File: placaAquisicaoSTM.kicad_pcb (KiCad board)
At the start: 2 copper layers, 102 x 80 mm, 82 parts, among them IC1 STM32H523CET6, J1 Conn_01x05, J2 Conn_02x06_Top_Bottom, SW1 SW_SPDT, SW2 SW_Push, U1 PC817, U2 PC817, U3 PC817, U4 LMV321, U5 LMV321, U6 74HC14, U7 AMS1117-5.0, U8 AMS1117-3.3, U9 SN65HVD230, Y1 Crystal, Y2 Crystal_GND23

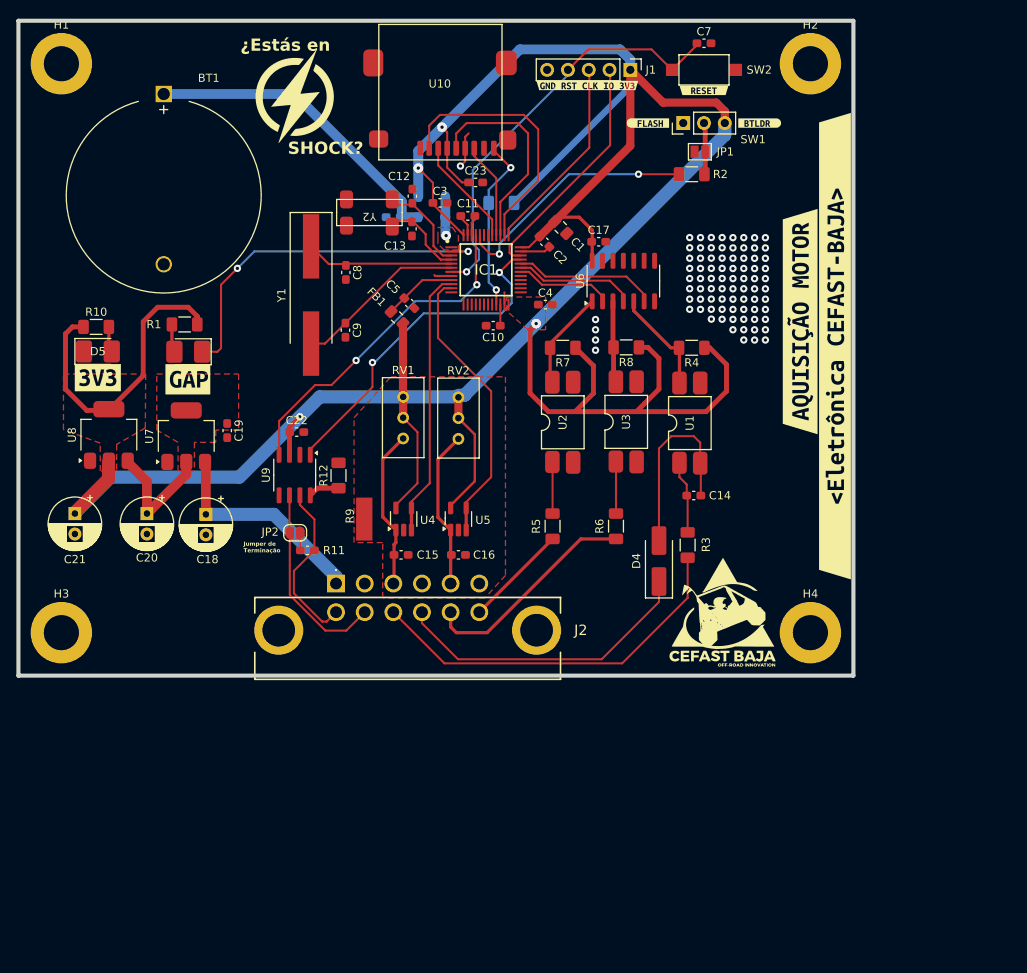
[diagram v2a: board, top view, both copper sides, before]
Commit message: Diminui o tamanho da placa
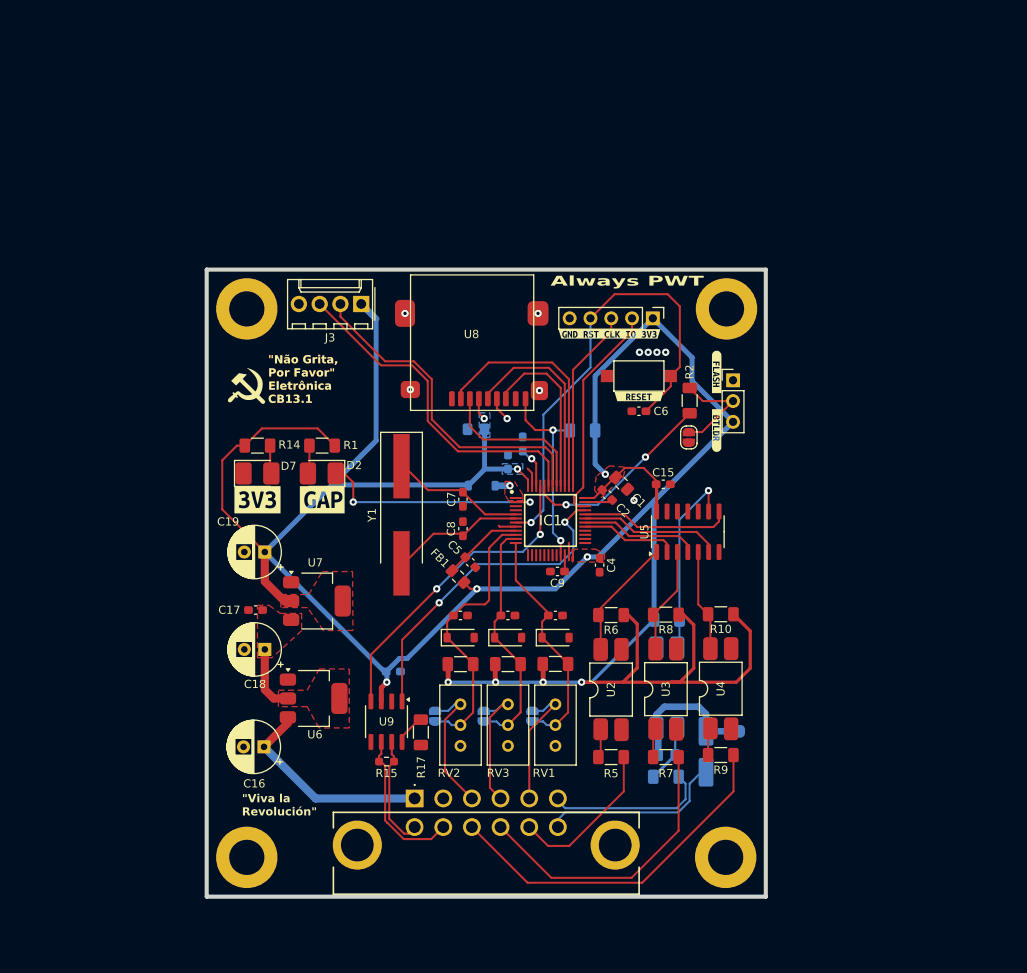
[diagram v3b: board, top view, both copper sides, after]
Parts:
- removed BT1: Battery_Cell, Battery:BatteryHolder_MYOUNG_BS-07-A1BJ001_CR2032
- removed the C12 at (111.6, 66.4)
- removed the C16 at (117.2, 110.2)
- removed C23: 1n, Capacitor_SMD:C_0603_1608Metric_Pad1.08x0.95mm_HandSolder
- removed the C6 at (109.3, 69.0)
- removed the D2 at (114.0, 69.0)
- removed the G*** at (97.2, 54.2)
- removed the G*** at (149.5, 117.2)
- removed the G*** at (142.8, 106.0)
- removed U10: ~, Baja_Library:SD-CARD-GENERIC
- removed the U5 at (117.2, 105.9)
- removed Y2: Crystal_GND23, Baja_Library:DMX-26S
- removed kibuzzard-6758F1AD: G***, kibuzzard-6758F1AD
- removed kibuzzard-6758F709: G***, kibuzzard-6758F709
- removed kibuzzard-6758F727: G***, kibuzzard-6758F727
- removed kibuzzard-67891694: G***, kibuzzard-67891694
- removed kibuzzard-67897D6F: G***, kibuzzard-67897D6F
- added C14: 1n, Capacitor_SMD:C_0603_1608Metric_Pad1.08x0.95mm_HandSolder, F.Cu at (129.1, 117.7)
- added C20: 1n, Capacitor_SMD:C_0805_2012Metric_Pad1.18x1.45mm_HandSolder, B.Cu at (119.4, 94.9)
- added D4: D_Zener, Diode_SMD:D_SOD-123, F.Cu at (117.5, 120.4)
- added D5: D_Zener, Diode_SMD:D_SOD-123, F.Cu at (123.3, 120.4)
- added D6: D_Zener, Diode_SMD:D_SOD-123, F.Cu at (129.1, 120.4)
- added G***: LOGO, Baja_Library:communism, F.Cu at (91.3, 89.6)
- added J3: Conn_01x04, Baja_Library:Molex_KK-254_AE-6410-04A_1x04_P2.54mm_Vertical, F.Cu at (105.4, 79.6)
- added JP6: SolderJumper_2_Open, Jumper:SolderJumper-2_P1.3mm_Open_RoundedPad1.0x1.5mm, B.Cu at (114.4, 129.9)
- added JP7: SolderJumper_2_Open, Jumper:SolderJumper-2_P1.3mm_Open_RoundedPad1.0x1.5mm, B.Cu at (120.3, 129.9)
- added JP8: SolderJumper_2_Open, Jumper:SolderJumper-2_P1.3mm_Open_RoundedPad1.0x1.5mm, B.Cu at (126.3, 129.9)
- added R10: 10k, Resistor_SMD:R_1206_3216Metric_Pad1.30x1.75mm_HandSolder, F.Cu at (149.3, 117.5)
- added R12: 27k, Resistor_SMD:R_1206_3216Metric_Pad1.30x1.75mm_HandSolder, F.Cu at (123.3, 123.6)
- added R15: 120, Resistor_SMD:R_0603_1608Metric_Pad0.98x0.95mm_HandSolder, F.Cu at (108.5, 135.5)
- added R16: 10K, Resistor_SMD:R_1206_3216Metric_Pad1.30x1.75mm_HandSolder, B.Cu at (132.4, 95.0)
- added RV3: 10k_trim, Potentiometer_THT:Potentiometer_Bourns_3296W_Vertical, F.Cu at (123.3, 128.5)
- added U8: ~, Baja_Library:SD-CARD-GENERIC, F.Cu at (118.8, 86.1)
- added kibuzzard-67EDAA6F: G***, kibuzzard-67EDAA6F, F.Cu at (100.6, 103.5)
- C10: renamed from C11; moved to B.Cu
- C11: renamed from C14; footprint Capacitor_SMD:C_0603_1608Metric_Pad1.08x0.95mm_HandSolder -> Capacitor_SMD:C_0805_2012Metric_Pad1.18x1.45mm_HandSolder; moved to B.Cu
- C13: value 22p -> 1n
- C21: renamed from C22; moved to B.Cu
- C3, H3, JP2, R3, R4, U1: moved to B.Cu
- D3: renamed from D4; moved to B.Cu
- JP1: footprint Jumper:SolderJumper-2_P1.3mm_Open_Pad1.0x1.5mm -> Jumper:SolderJumper-2_P1.3mm_Open_RoundedPad1.0x1.5mm
- R11: value 120 -> 27k; footprint Capacitor_SMD:C_0603_1608Metric_Pad1.08x0.95mm_HandSolder -> Resistor_SMD:R_1206_3216Metric_Pad1.30x1.75mm_HandSolder
- R13: value 10k -> 27k; moved to F.Cu
- R9: value 0R -> 680; footprint Baja_Library:JumperPotencia -> Resistor_SMD:R_1206_3216Metric_Pad1.30x1.75mm_HandSolder
- U4: value LMV321 -> PC817; footprint Package_TO_SOT_SMD:SOT-23-5_HandSoldering -> Baja_Library:SO-4_HandSoldering
- moved JP2 59.0 mm to (151.1, 131.8)
- moved R13 56.7 mm to (129.1, 123.6)
- moved R9 52.3 mm to (149.3, 134.7), turned to 180 degrees
- moved C13 48.7 mm to (123.3, 117.7), turned to 0 degrees
- moved G*** 47.4 mm to (96.7, 88.4)
- moved C6 45.6 mm to (139.3, 92.7), turned to 180 degrees
- moved U4 43.9 mm to (149.3, 126.6)
- moved RV1 41.9 mm to (129.1, 128.5)
- moved SW2 38.2 mm to (139.3, 88.4), turned to 0 degrees
- moved kibuzzard-67572B0D 38.2 mm to (139.3, 90.9)
- moved kibuzzard-67572AD3 37.9 mm to (148.8, 95.1), turned to -90 degrees
- moved H1 37.6 mm to (91.4, 80.2)
- moved RV2 37.5 mm to (117.5, 128.5)
- moved D1 35.8 mm to (120.1, 101.8)
- moved U6 35.6 mm to (99.6, 127.8), turned to 0 degrees
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- renumbered C15 to C12, C17 to C15, C18 to C16, C19 to C17, C20 to C18, C21 to C19, C7 to C6, C8 to C7, C9 to C8, C10 to C9, D3 to D2, D5 to D7, R10 to R14, R12 to R17, R7 to R6, R6 to R7, U6 to U5, U7 to U6, U8 to U7
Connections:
- C11 pad 2: Net-(D4-A) -> JMP_RPM
- C12 pad 1: NTC_P1 -> NTC_AN_1
- C12 pad 2: NTC_N1 -> GND
- C13 pad 1: /MicroControlador/LSE_OUT -> NTC_AN_2
- D3 pad 1: MTMT -> MT+
- D3 pad 2: Net-(D4-A) -> JMP_RPM
- IC1 pad 12: unconnected-(IC1-PA2-Pad12) -> NTC_AN_3
- IC1 pad 21: SD_ON -> SD_DET
- IC1 pad 29: unconnected-(IC1-PA8-Pad29) -> DIG3
- IC1 pad 3: /MicroControlador/LSE_IN -> unconnected-(IC1-PC14-OSC32_IN-Pad3)
- IC1 pad 38: CS_SD -> SD_CS
- IC1 pad 4: /MicroControlador/LSE_OUT -> unconnected-(IC1-PC15-OSC32_OUT-Pad4)
- J2 pad 10: MTMT -> OPTO_IN_1
- J2 pad 11: OPTO_IN_1 -> OPTO_IN_0
- J2 pad 12: OPTO_IN_0 -> MT+
- J2 pad 4: NTC_N1 -> NTC_P2
- J2 pad 5: NTC_P2 -> NTC_P3
- J2 pad 6: NTC_N1 -> MT-
- J2 pad 9: CHASSI -> OPTO_IN_2
- JP2 pad 1: CAN- -> JMP_RPM
- JP2 pad 2: Net-(JP2-B) -> GND
- R11 pad 1: CAN+ -> +3V3
- R11 pad 2: Net-(JP2-B) -> NTC_AN_1
- R13 pad 1: SD_ON -> +3V3
- R13 pad 2: +3V3 -> NTC_AN_3
- R3 pad 1: CHASSI -> MT-
- R9 pad 1: GND -> OPTO_IN_2
- R9 pad 2: NTC_N1 -> Net-(R9-Pad2)
- RV1 pad 1: +3V3 -> NTC_P3
- RV1 pad 2: +3V3 -> NTC_AN_3
- RV1 pad 3: NTC_P1 -> GND
- RV2 pad 1: +3V3 -> NTC_P1
- RV2 pad 2: +3V3 -> NTC_AN_1
- RV2 pad 3: NTC_P2 -> GND
- U1 pad 2: Net-(D4-A) -> JMP_RPM
- U4 pad 1: NTC_P1 -> Net-(R9-Pad2)
- U4 pad 2: NTC_N1 -> GND
- U4 pad 3: NTC_AN_1 -> GND
- U4 pad 4: NTC_AN_1 -> OPTO_2
- U5 pad 2: DIG2 -> DIG3
- U5 pad 4: DIG1 -> DIG2
- U5 pad 5: RPM -> OPTO_2
- U5 pad 6: DIG0 -> DIG1
- U5 pad 8: (no net) -> DIG0
- U5 pad 9: (no net) -> RPM
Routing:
- net CHASSI: track 46.8 -> 0.00 mm
- net OPTO_IN_2: track 0.00 -> 43.8 mm
- net RX1: track 0.00 -> 41.8 mm
- net TX1: track 0.00 -> 41.1 mm
- net Net-(BT1-+): track 38.5 -> 0.00 mm
- net MTMT: track 37.5 -> 0.00 mm
- net CS_SD: track 32.0 -> 0.00 mm
- net SD_CS: track 0.00 -> 29.5 mm
- net NTC_AN_3: track 0.00 -> 29.1 mm
- net SD_DET: track 0.00 -> 24.2 mm, vias 0 -> 2
- net Net-(D4-A): track 23.7 -> 0.00 mm
- net MT+: track 0.00 -> 22.6 mm
- net SD_ON: track 21.4 -> 0.00 mm, vias 2 -> 0
- net MT-: track 0.00 -> 19.8 mm
- net JMP_RPM: track 0.00 -> 16.9 mm
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- added copper zone on B.Cu, net +3V3
- removed copper zone on F.Cu, net NTC_N1
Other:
- board size 102 x 80 mm -> 68.3 x 76.6 mm
- board text added: "Always PWT"
- board text added: "{dblquote}Não Grita, Por Favor{dblquote} Eletrônica CB13.1"
- board text added: "{dblquote}Se eu ouvisse o que eles dizem não fazia nada, O que eles dizem não derruba minha parada{dblquote}"
- board text added: "{dblquote}Viva la Revolución{dblquote}"
- board text removed: "I LOVE PWT"
- board text removed: "Jumper de Terminação"
- board text removed: "SHOCK?"
- board text removed: "¿Estás en"

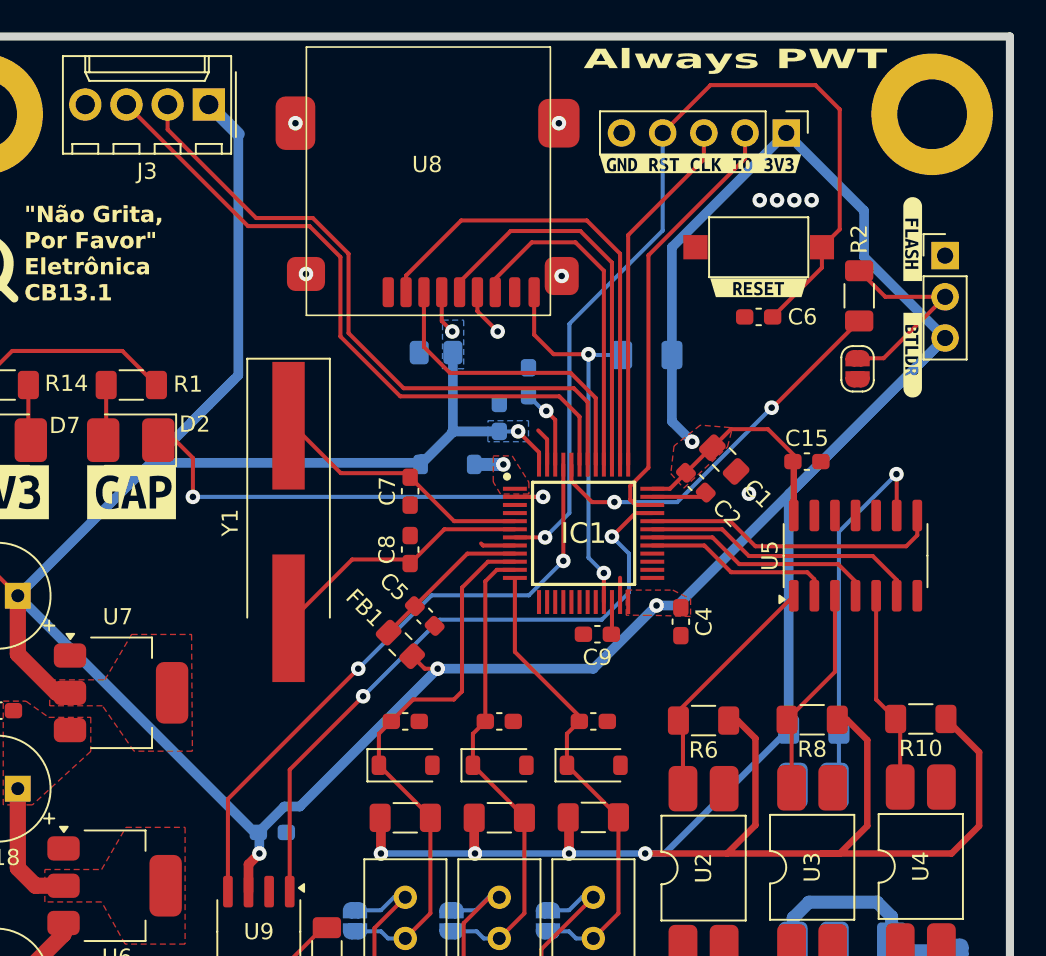
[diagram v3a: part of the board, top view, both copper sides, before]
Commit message: Removi o botao de reset do design
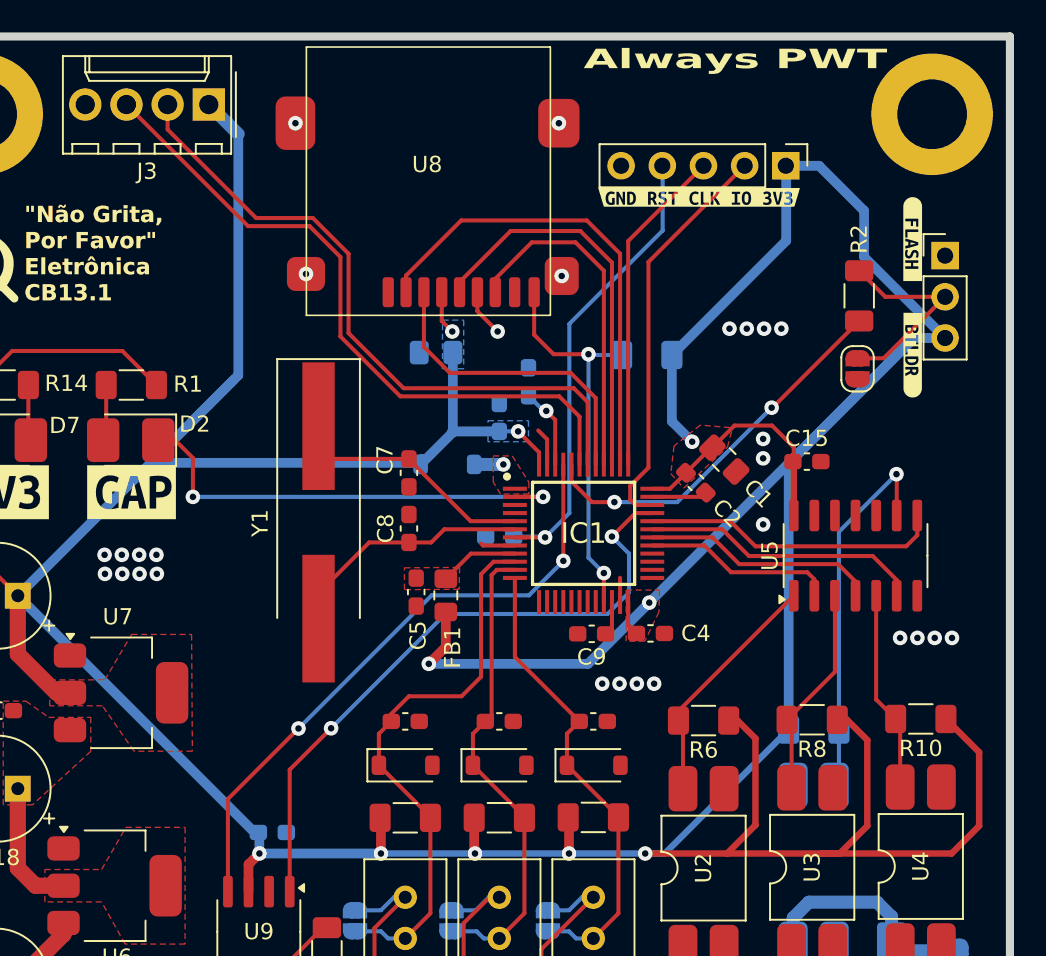
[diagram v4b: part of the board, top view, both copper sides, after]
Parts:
- removed SW2: SW_Push, Button_Switch_SMD:SW_SPST_CK_RS282G05A3
- removed kibuzzard-67572B0D: G***, kibuzzard-67572B0D
- C6: moved to B.Cu
- moved C6 20.9 mm to (123.3, 106.2)
- moved FB1 4.12 mm to (120.0, 109.9), turned to 90 degrees
- moved kibuzzard-6758FD86 2.08 mm to (135.6, 85.3)
- moved J1 2.03 mm to (141.0, 83.4)
- moved C4 2.01 mm to (132.6, 112.2), turned to 0 degrees
- moved Y1 1.85 mm to (112.2, 105.4)
- moved C5 1.57 mm to (118.2, 109.7), turned to -90 degrees
- moved C8 1.30 mm to (117.7, 105.8)
- moved C7 1.13 mm to (117.7, 102.3)
- moved C9 0.35 mm to (129.0, 112.2)
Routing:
- net /MicroControlador/NRST: track 57.1 -> 29.8 mm
- net +3V3: track 388.7 -> 382.1 mm
- net +3.3VA: track 9.82 -> 4.90 mm
- net /MicroControlador/SWDIO: track 27.1 -> 25.0 mm
- net /MicroControlador/SWCLK: track 22.4 -> 20.4 mm
- net /MicroControlador/HSE_IN: track 16.4 -> 15.4 mm
- net /MicroControlador/HSE_OUT: track 16.2 -> 15.3 mm
- net GND: vias 10 -> 28
- added copper zone on F.Cu, net +3.3VA

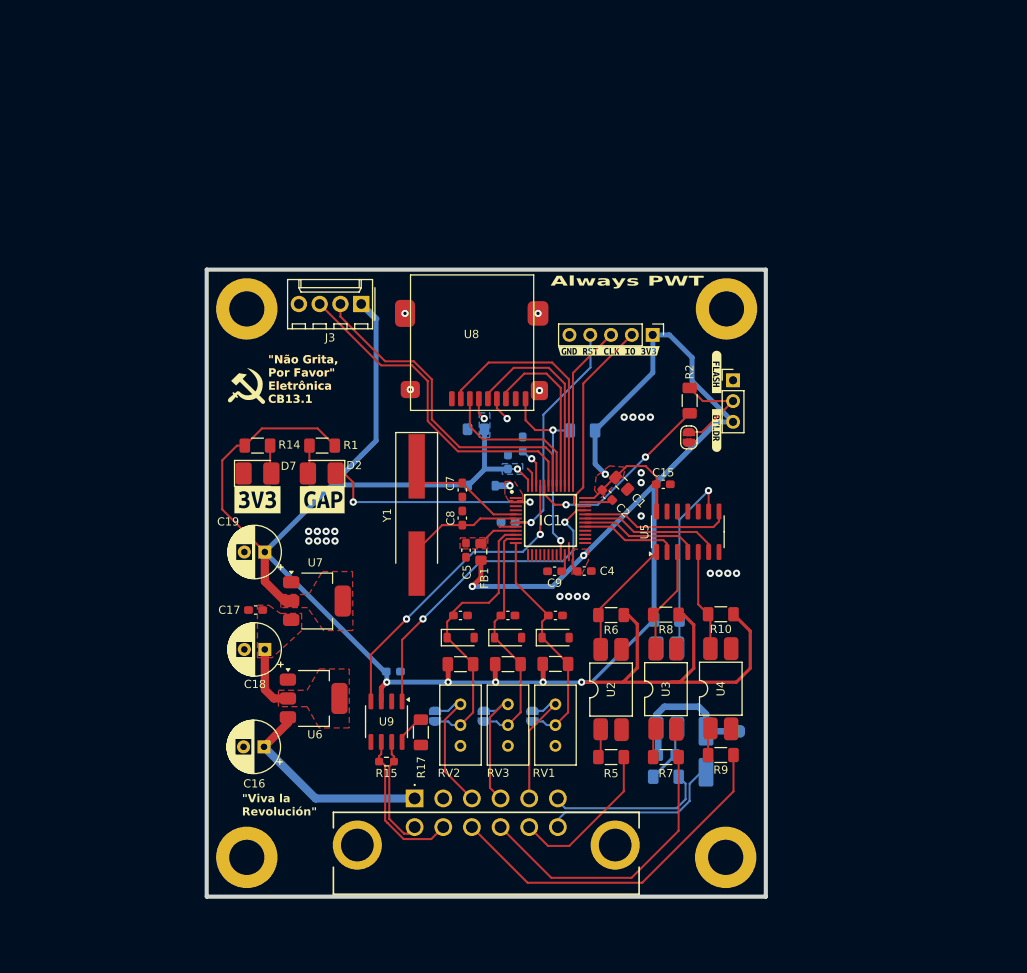
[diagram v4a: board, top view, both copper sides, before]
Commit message: Troquei o conector para o conector DEUTSCH
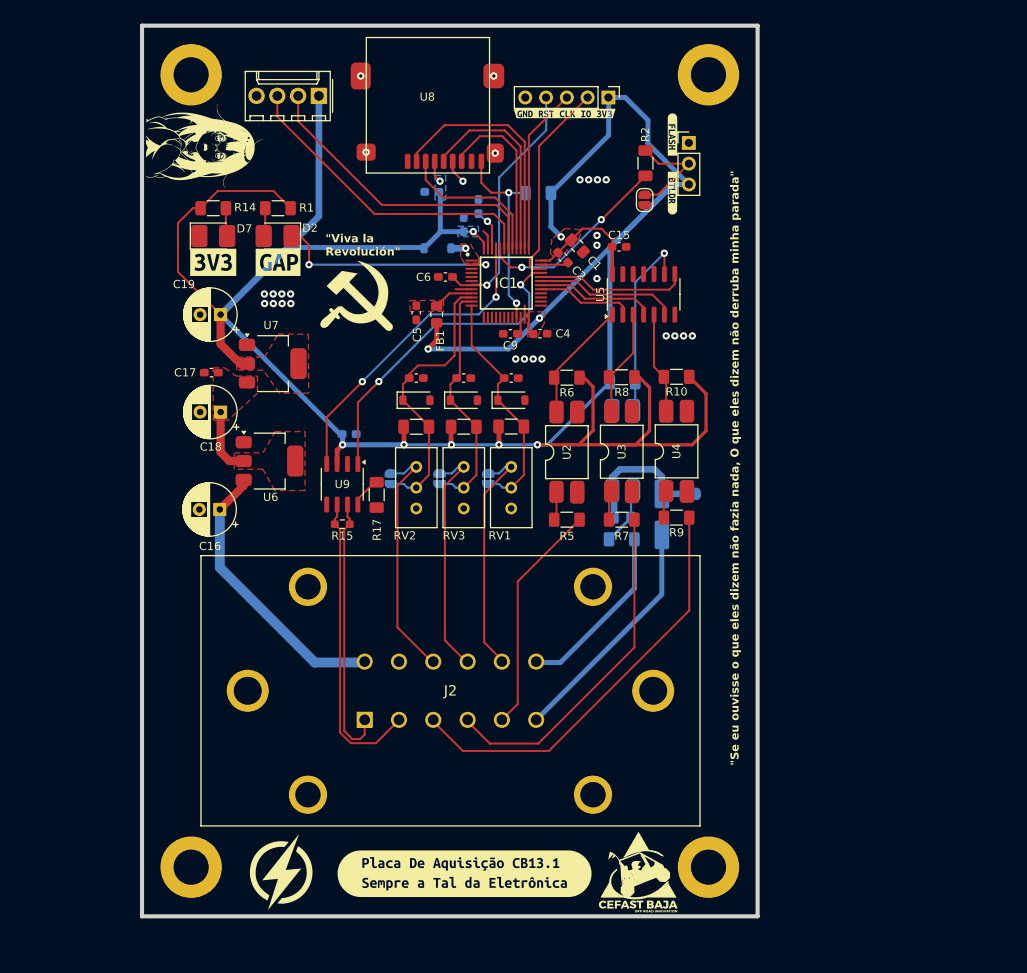
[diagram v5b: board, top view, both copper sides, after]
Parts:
- removed C7, C8: 22p, Capacitor_SMD:C_0603_1608Metric_Pad1.08x0.95mm_HandSolder
- removed Y1: Crystal, Crystal:Crystal_SMD_HC49-SD_HandSoldering
- added G***: LOGO, Baja_Library:Jumper_Potencia, F.Cu at (87.2, 62.4)
- added G***: LOGO, Baja_Library:Raio_Circulo, F.Cu at (95.6, 149.0)
- added kibuzzard-683E47A0: G***, kibuzzard-683E47A0, F.Cu at (118.0, 149.2)
- C20: footprint Capacitor_SMD:C_0805_2012Metric_Pad1.18x1.45mm_HandSolder -> Capacitor_SMD:C_0603_1608Metric_Pad1.08x0.95mm_HandSolder
- C6, G***: moved to F.Cu
- J2: value Conn_02x06_Top_Bottom -> Conn_02x06_Counter_Clockwise; footprint Baja_Library:MX120G -> Baja_Library:DTM1512PA
- R16: value 10K -> 10k
- moved G*** 74.0 mm to (139.2, 149.0), turned to 0 degrees
- moved C6 30.9 mm to (115.7, 76.3)
- moved C5 29.6 mm to (112.1, 80.7)
- moved D3 29.5 mm to (142.1, 105.3)
- moved JP2 29.5 mm to (145.7, 102.8)
- moved R17 29.5 mm to (107.3, 102.9)
- moved R2 29.5 mm to (140.1, 62.4)
- moved kibuzzard-67572A93 29.5 mm to (143.4, 58.9)
- moved C1 29.5 mm to (131.8, 72.5)
- moved C12 29.5 mm to (112.1, 88.7)
- moved C15 29.5 mm to (136.9, 72.6)
- moved C2 29.5 mm to (130.0, 73.9)
- moved C20 29.5 mm to (114.0, 65.9)
- moved C4 29.5 mm to (127.2, 83.2)
- moved C9 29.5 mm to (123.6, 83.2)
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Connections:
- J2 pad 1: +12V -> CAN+
- J2 pad 10: OPTO_IN_1 -> NTC_P1
- J2 pad 11: OPTO_IN_0 -> GND
- J2 pad 12: MT+ -> +12V
- J2 pad 2: GND -> CAN-
- J2 pad 3: NTC_P1 -> OPTO_IN_2
- J2 pad 4: NTC_P2 -> OPTO_IN_1
- J2 pad 5: NTC_P3 -> OPTO_IN_0
- J2 pad 6: MT- -> MT+
- J2 pad 7: CAN+ -> MT-
- J2 pad 8: CAN- -> NTC_P3
- J2 pad 9: OPTO_IN_2 -> NTC_P2
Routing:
- net CAN+: track 13.9 -> 33.0 mm
- net CAN-: track 18.8 -> 37.2 mm
- net /MicroControlador/HSE_IN: track 15.4 -> 0.00 mm
- net /MicroControlador/HSE_OUT: track 15.3 -> 0.00 mm
- net NTC_P3: track 16.0 -> 29.2 mm
- net NTC_P1: track 17.1 -> 30.1 mm
- net NTC_P2: track 16.6 -> 29.3 mm
- net OPTO_IN_0: track 19.5 -> 28.4 mm
- net +12V: track 25.8 -> 34.5 mm
- net OPTO_IN_2: track 43.8 -> 51.4 mm
- net OPTO_IN_1: track 35.7 -> 42.1 mm
- net MT+: track 22.6 -> 29.0 mm
- net TX1: track 41.1 -> 37.5 mm
- net RX1: track 41.8 -> 38.7 mm
- net /MicroControlador/NRST: track 29.8 -> 32.5 mm
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- added copper zone on B.Cu, net (none)
- added copper zone on F.Cu, net (none)
- removed copper zone on B.Cu, net +3V3
- removed copper zone on F.Cu, net /MicroControlador/VBAT
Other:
- board size 68.3 x 76.6 mm -> 75.2 x 108.8 mm
- board text removed: "Always PWT"
- board text removed: "{dblquote}Não Grita, Por Favor{dblquote} Eletrônica CB13.1"
